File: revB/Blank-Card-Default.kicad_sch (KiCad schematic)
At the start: 24 parts, among them Q301 MMBT4403M3T5G, Q302 BC847BM3T5G, Q303 BC847BM3T5G, Q304 BC847BM3T5G

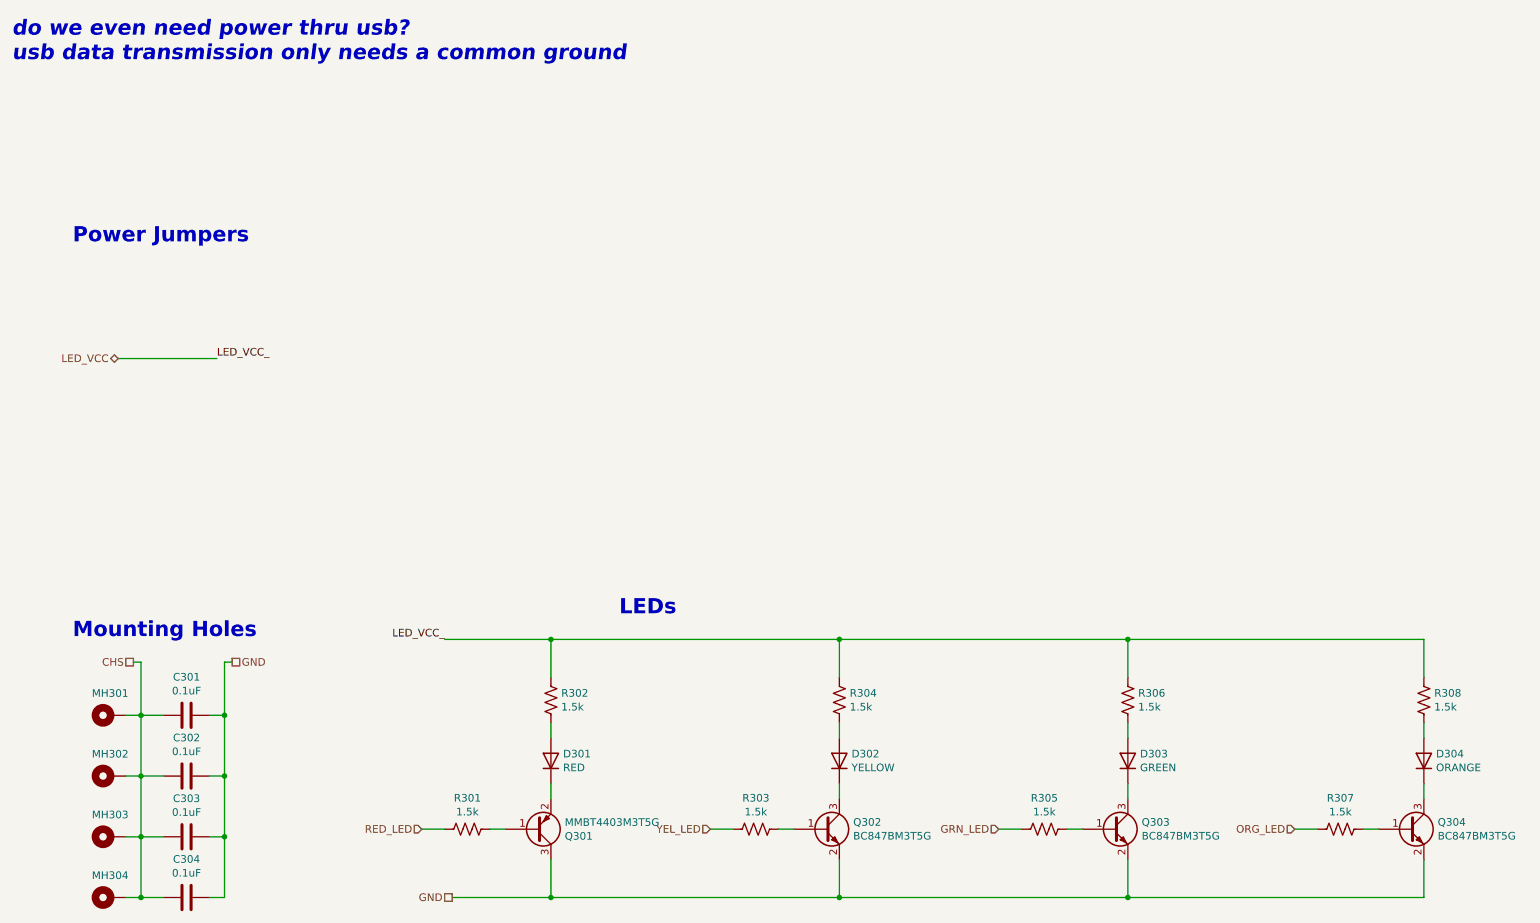
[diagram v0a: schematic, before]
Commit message: update project to kicad 7 format
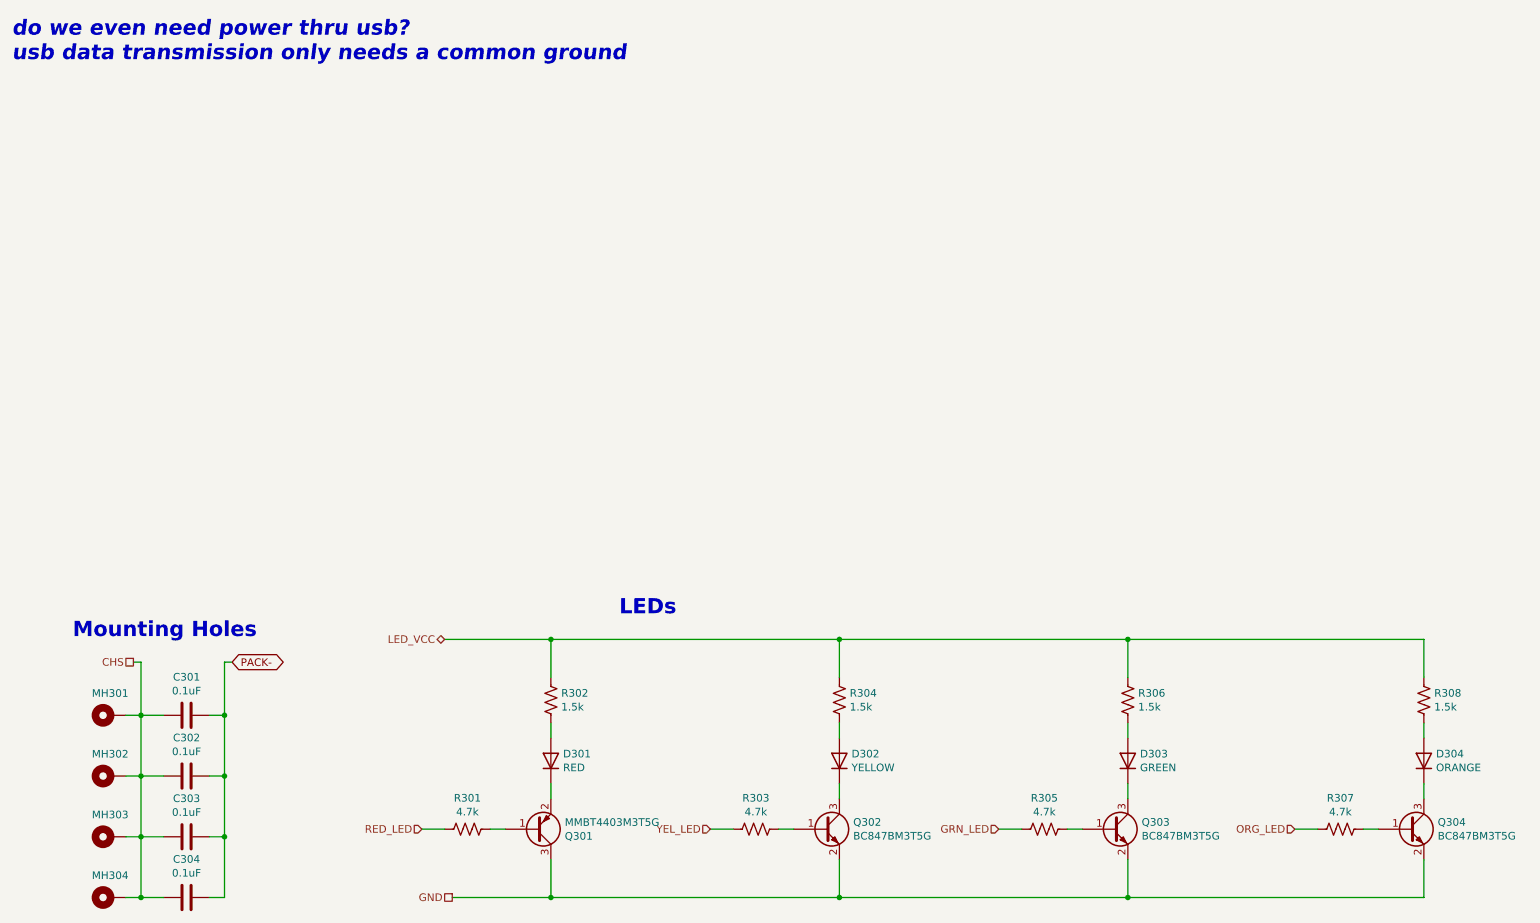
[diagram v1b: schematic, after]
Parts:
- R301, R303, R305, R307: value 1.5k -> 4.7k
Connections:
- net GND: no longer C301.1, C302.1, C303.1, C304.1
- new net PACK-: C301.1, C302.1, C303.1, C304.1
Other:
- note removed: "Power Jumpers"
